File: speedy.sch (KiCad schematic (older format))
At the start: 162 parts, among them IC1 TC4424EPA, IC3 VR, IC4 SP721, IC5 LTV827, IC7 TC4424EPA, IC8 TC4424EPA, J1 Conn_02x21_Counter_Clockwise, J2 CONN_01X26, Q1 STP62NS04Z, Q10 BC547(b), Q2 STP62NS04Z, Q3 STP62NS04Z, Q4 STP62NS04Z, Q5 STP62NS04Z, Q6 STP62NS04Z, Q7 STP62NS04Z, Q8 STP62NS04Z, Q9 VP3203N3-G, U1 L4940-5V

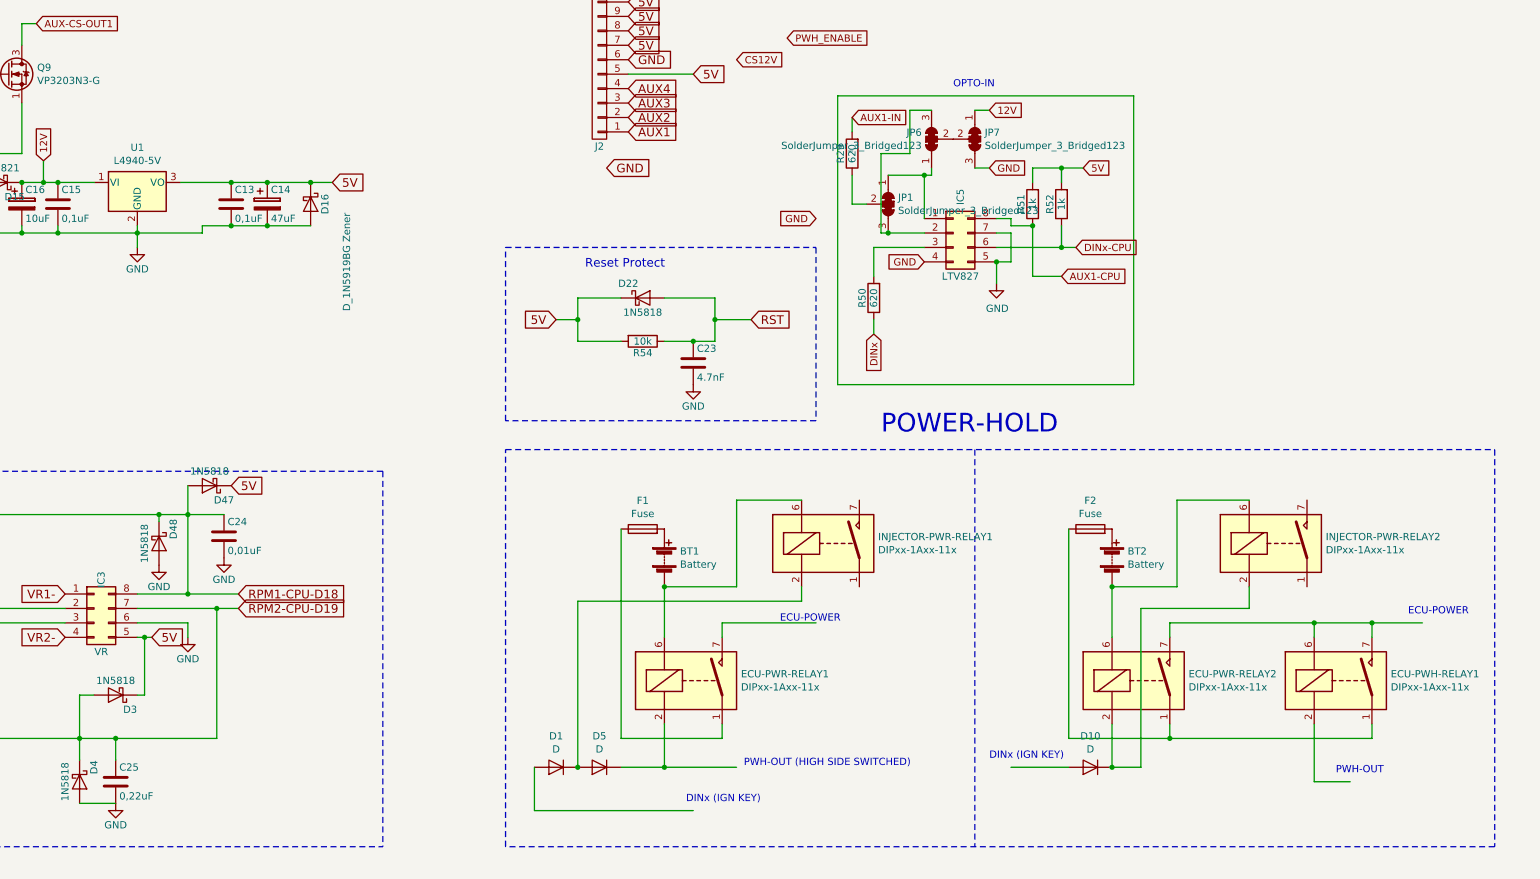
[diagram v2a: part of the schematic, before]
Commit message: Updated bom and footprint in ULN
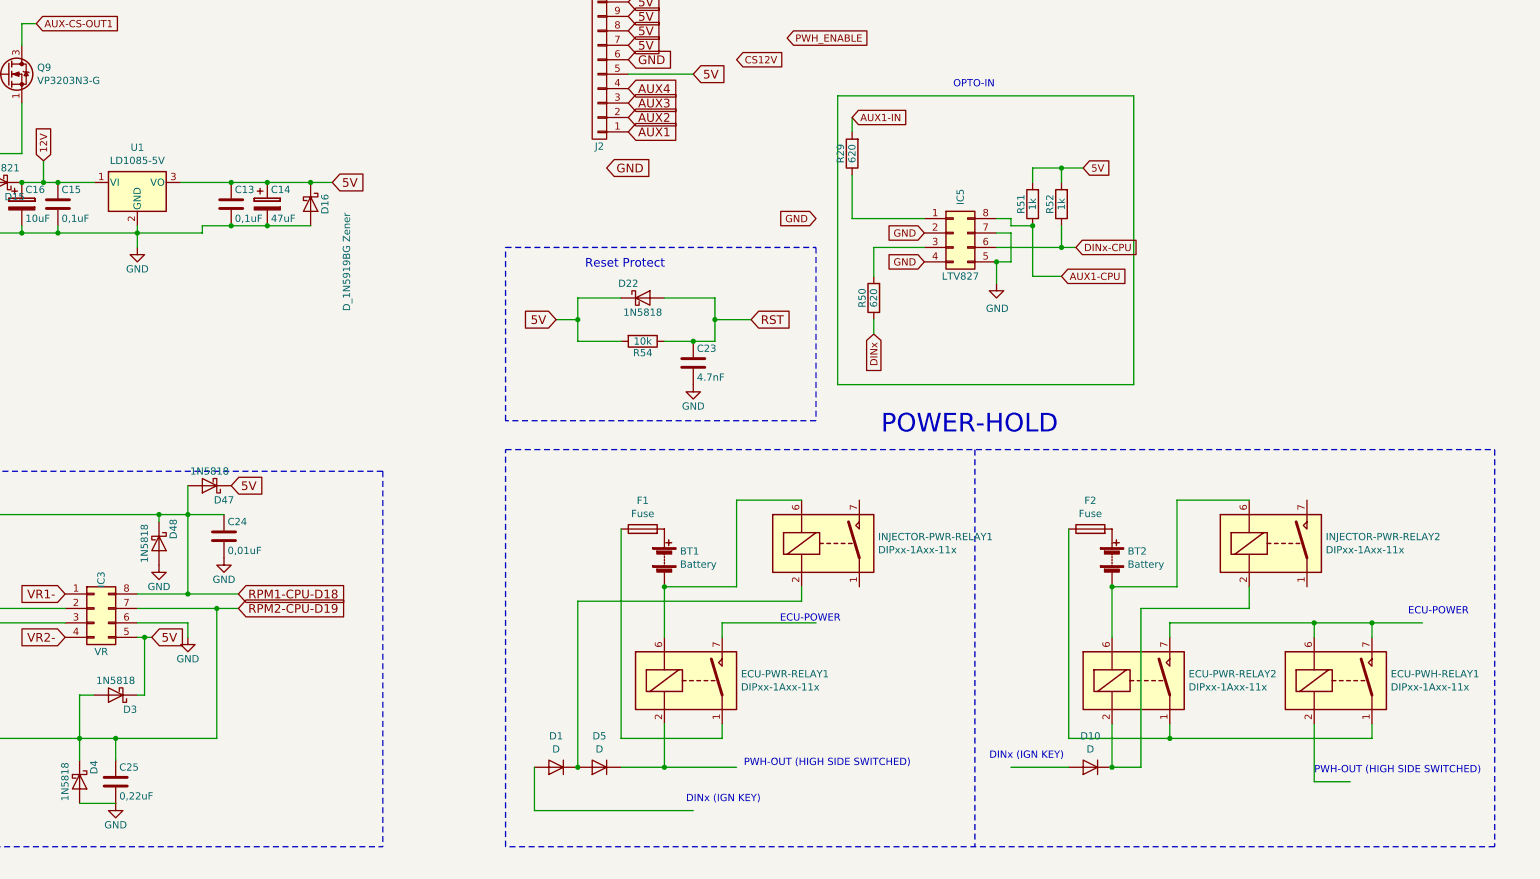
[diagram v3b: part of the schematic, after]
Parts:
- removed JP1, JP6, JP7: SolderJumper_3_Bridged123, Jumper:SolderJumper-3_P1.3mm_Open_RoundedPad1.0x1.5mm_NumberLabels, symbol Jumper:SolderJumper_3_Bridged123
- U1: value L4940-5V -> LD1085-5V
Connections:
- net GND: now also IC5.2 (Pin_2)
- net at IC5.1 (Pin_1): now also R29.1
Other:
- note removed: "PWH-OUT"
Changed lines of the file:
@@
 EESchema Schematic File Version 4
 LIBS:speedy-cache
-EELAYER 29 0
+EELAYER 30 0
 EELAYER END
 $Descr A4 11693 8268
@@
 Wire Wire Line
 	16750 9900 16750 9800
-Text Notes 17900 10150 0    50   ~ 0
-PWH-OUT
+Text Notes 17750 10150 0    50   ~ 0
+PWH-OUT (HIGH SIDE SWITCHED)
 $Comp
 L Device:Fuse F2
@@
 PWR
 Wire Wire Line
-	14800 6400 15050 6400
-Wire Wire Line
 	14450 5450 14450 7450
-Wire Wire Line
-	15050 6300 15050 6000
-Wire Wire Line
-	15050 6000 14800 6000
-Wire Wire Line
-	14550 6000 14550 6200
-$Comp
-L Jumper:SolderJumper_3_Bridged123 JP6
-U 1 1 5C84A0FF
-P 15100 5750
-F 0 "JP6" V 15146 5818 50  0000 L CNN
-F 1 "SolderJumper_3_Bridged123" V 15055 5818 50  0000 L CNN
-F 2 "Jumper:SolderJumper-3_P1.3mm_Open_RoundedPad1.0x1.5mm_NumberLabels" H 15100 5750 50  0001 C CNN
-F 3 "~" H 15100 5750 50  0001 C CNN
-	1    15100 5750
-	0    -1   -1   0
-$EndComp
-Wire Wire Line
-	14550 6200 14650 6200
-$Comp
-L Jumper:SolderJumper_3_Bridged123 JP1
-U 1 1 5C7C38D3
-P 14800 6200
-F 0 "JP1" V 14754 6268 50  0000 L CNN
-F 1 "SolderJumper_3_Bridged123" V 14845 6268 50  0000 L CNN
-F 2 "Jumper:SolderJumper-3_P1.3mm_Open_RoundedPad1.0x1.5mm_NumberLabels" H 14800 6200 50  0001 C CNN
-F 3 "~" H 14800 6200 50  0001 C CNN
-	1    14800 6200
-	0    1    1    0
-$EndComp
-Wire Wire Line
-	15100 5550 14950 5550
-Wire Wire Line
-	14950 5550 14950 5850
-Wire Wire Line
-	14950 5850 14750 5850
-Wire Wire Line
-	14750 5850 14750 6400
-Wire Wire Line
-	14750 6400 14800 6400
-Connection ~ 14800 6400
-Wire Wire Line
-	15100 5950 15100 6000
-Wire Wire Line
-	15100 6000 15050 6000
-Connection ~ 15050 6000
-$Comp
-L Jumper:SolderJumper_3_Bridged123 JP7
-U 1 1 5C9D3331
-P 15400 5750
-F 0 "JP7" V 15354 5818 50  0000 L CNN
-F 1 "SolderJumper_3_Bridged123" V 15445 5818 50  0000 L CNN
-F 2 "Jumper:SolderJumper-3_P1.3mm_Open_RoundedPad1.0x1.5mm_NumberLabels" H 15400 5750 50  0001 C CNN
-F 3 "~" H 15400 5750 50  0001 C CNN
-	1    15400 5750
-	0    1    1    0
-$EndComp
-Text GLabel 15500 5950 2    50   Input ~ 0
+Text GLabel 15050 6400 0    50   Input ~ 0
 GND
-Text GLabel 15500 5550 2    50   Input ~ 0
-12V
-Wire Wire Line
-	15400 5550 15500 5550
-Wire Wire Line
-	15400 5950 15500 5950
 $Comp
 L Transistor_BJT:BC547 Q10
@@
 P 9600 6050
 F 0 "U1" H 9600 6292 50  0000 C CNN
-F 1 "L4940-5V" H 9600 6201 50  0000 C CNN
+F 1 "LD1085-5V" H 9600 6201 50  0000 C CNN
 F 2 "Package_TO_SOT_THT:TO-220-3_Vertical" H 9600 6275 50  0001 C CIN
 F 3 "http://www.fairchildsemi.com/ds/LM/LM78M05.pdf" H 9600 6000 50  0001 C CNN
@@
 Text GLabel 4350 4800 0    50   Input ~ 0
 ULN-BOOST
+Wire Wire Line
+	14550 6000 14550 6300
+Wire Wire Line
+	14550 6300 15050 6300
 $EndSCHEMATC
